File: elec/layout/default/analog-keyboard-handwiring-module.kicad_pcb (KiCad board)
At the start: 2 copper layers, 95.2 x 95.2 mm, 289 parts, among them J1 Conn_01x04, J10 Conn_01x02, J100 Conn_01x04, J11 Conn_01x01, J12 Conn_01x04, J13 Conn_01x04, J14 Conn_01x02, J15 Conn_01x01, J16 Conn_01x04, J17 Conn_01x04, J18 Conn_01x02, J19 Conn_01x01, J2 Conn_01x02, J20 Conn_01x04, J21 Conn_01x04, J22 Conn_01x02, J23 Conn_01x01, J24 Conn_01x04, J25 Conn_01x04, J26 Conn_01x02, J27 Conn_01x01, J28 Conn_01x04, J29 Conn_01x04, J3 Conn_01x01, J30 Conn_01x02, J31 Conn_01x01, J32 Conn_01x04, J33 Conn_01x04, J34 Conn_01x02, J35 Conn_01x01, J36 Conn_01x04, J37 Conn_01x04, J38 Conn_01x02, J39 Conn_01x01, J4 Conn_01x04, J40 Conn_01x04, J41 Conn_01x04, J42 Conn_01x02, J43 Conn_01x01, J44 Conn_01x04, J45 Conn_01x04, J46 Conn_01x02, J47 Conn_01x01, J48 Conn_01x04, J49 Conn_01x04, J5 Conn_01x04, J50 Conn_01x02, J51 Conn_01x01, J52 Conn_01x04, J53 Conn_01x04, J54 Conn_01x02, J55 Conn_01x01, J56 Conn_01x04, J57 Conn_01x04, J58 Conn_01x02, J59 Conn_01x01, J6 Conn_01x02, J60 Conn_01x04, J61 Conn_01x04, J62 Conn_01x02, J63 Conn_01x01, J64 Conn_01x04, J65 Conn_01x04, J66 Conn_01x02, J67 Conn_01x01, J68 Conn_01x04, J69 Conn_01x04, J7 Conn_01x01, J70 Conn_01x02, J71 Conn_01x01, J72 Conn_01x04, J73 Conn_01x04, J74 Conn_01x02, J75 Conn_01x01, J76 Conn_01x04, J77 Conn_01x04, J78 Conn_01x02, J79 Conn_01x01, J8 Conn_01x04, J80 Conn_01x04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

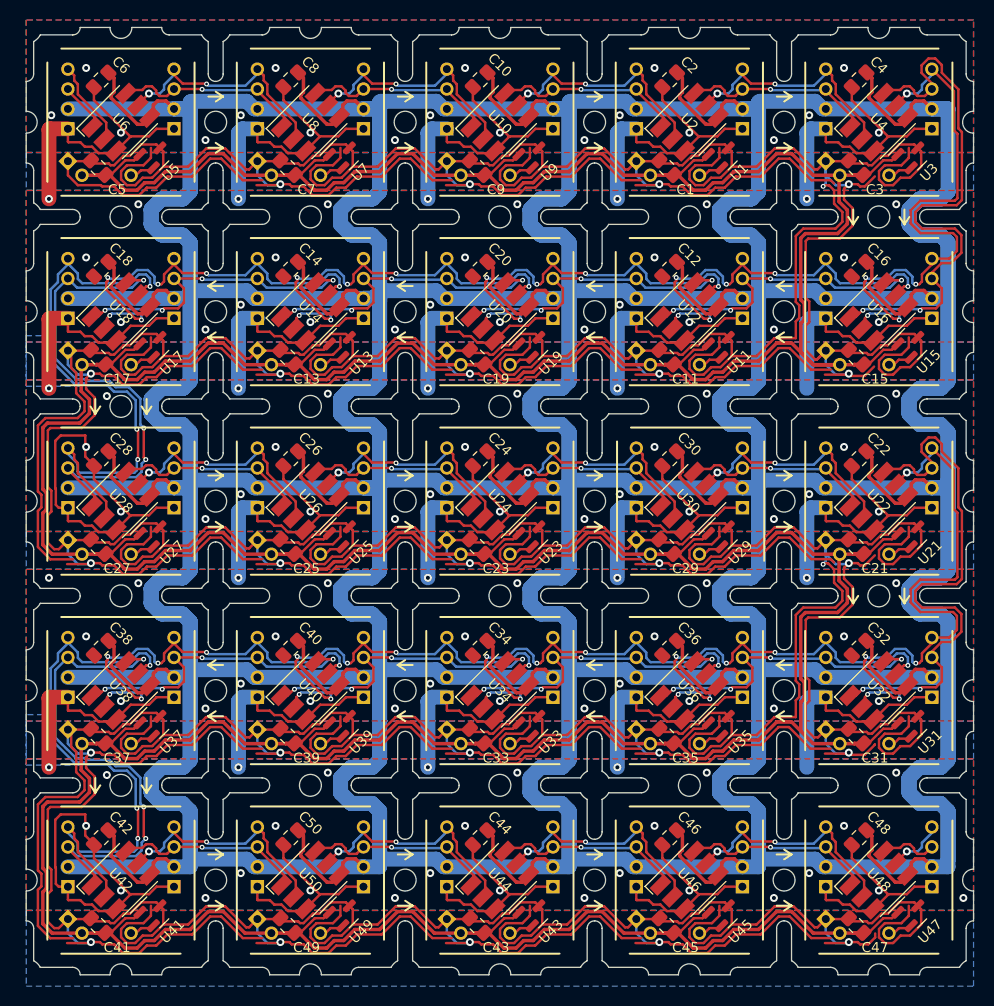
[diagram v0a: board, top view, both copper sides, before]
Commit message: Switch connectors and place components
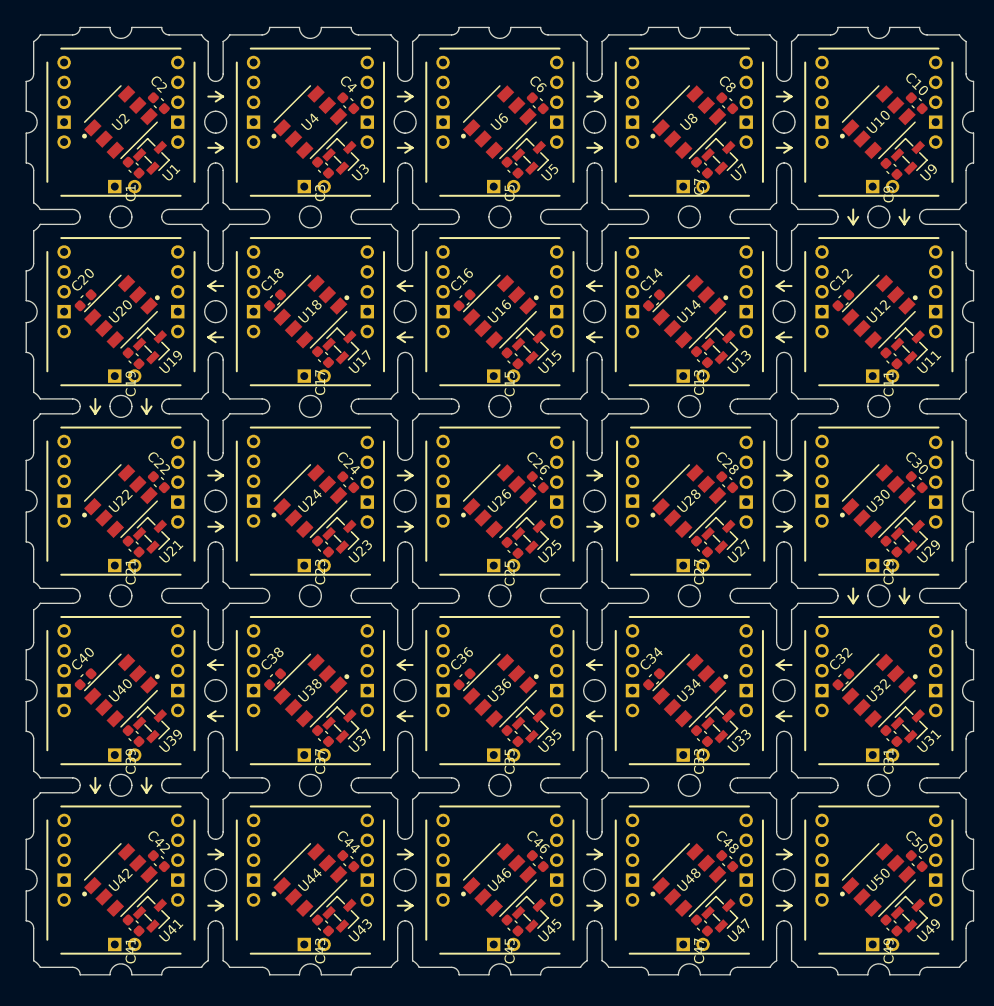
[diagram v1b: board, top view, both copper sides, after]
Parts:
- removed H1, H10, H11, H13, H14, H15, H16, H17, H19, H2, H20, H21, H22, H23, H24, H25, H26, H27, H28, H29, H3, H30, H31, H32, H33, H34, H35, H36, H37, H38, H39, H4, H40, H5, H6, H7, H8, H9, locked: MountingHole, MountingHole:MountingHole_2.2mm_M2
- removed H18: locked, MountingHole:MountingHole_2.2mm_M2
- removed the J10 at (92.3, 63.4)
- removed the J14 at (111.3, 63.4)
- removed the J18 at (130.4, 63.4)
- removed the J2 at (73.2, 63.4)
- removed the J22 at (130.4, 82.5)
- removed the J26 at (111.3, 82.5)
- removed the J30 at (92.3, 82.5)
- removed the J34 at (73.2, 82.5)
- removed the J38 at (54.2, 82.5)
- removed the J42 at (54.2, 101.5)
- removed the J46 at (73.2, 101.5)
- removed the J50 at (92.3, 101.5)
- removed the J54 at (111.3, 101.5)
- removed the J58 at (130.4, 101.5)
- removed the J6 at (54.2, 63.4)
- removed the J62 at (130.4, 120.6)
- removed the J66 at (111.3, 120.6)
- removed the J70 at (92.3, 120.6)
- removed the J74 at (73.2, 120.6)
- removed J78, J82, J86, J90, J94, J98: Conn_01x02, footprints:conn_2
- C1: renamed from C5; value 0.1µF -> 50V 100nF X7R ±10% 0603 Multilayer Ceramic Capacitors MLCC - SMD/SMT ROHS; footprint Capacitor_SMD:C_0805_2012Metric_Pad1.18x1.45mm_HandSolder -> lib:C0603
- C10: renamed from C4; value 0.1µF -> 50V 100nF X7R ±10% 0603 Multilayer Ceramic Capacitors MLCC - SMD/SMT ROHS; footprint Capacitor_SMD:C_0805_2012Metric_Pad1.18x1.45mm_HandSolder -> lib:C0603
- C11: renamed from C15; value 0.1µF -> 50V 100nF X7R ±10% 0603 Multilayer Ceramic Capacitors MLCC - SMD/SMT ROHS; footprint Capacitor_SMD:C_0805_2012Metric_Pad1.18x1.45mm_HandSolder -> lib:C0603
- C12: renamed from C16; value 0.1µF -> 50V 100nF X7R ±10% 0603 Multilayer Ceramic Capacitors MLCC - SMD/SMT ROHS; footprint Capacitor_SMD:C_0805_2012Metric_Pad1.18x1.45mm_HandSolder -> lib:C0603
- C13: renamed from C11; value 0.1µF -> 50V 100nF X7R ±10% 0603 Multilayer Ceramic Capacitors MLCC - SMD/SMT ROHS; footprint Capacitor_SMD:C_0805_2012Metric_Pad1.18x1.45mm_HandSolder -> lib:C0603
- C14: renamed from C12; value 0.1µF -> 50V 100nF X7R ±10% 0603 Multilayer Ceramic Capacitors MLCC - SMD/SMT ROHS; footprint Capacitor_SMD:C_0805_2012Metric_Pad1.18x1.45mm_HandSolder -> lib:C0603
- C15: renamed from C19; value 0.1µF -> 50V 100nF X7R ±10% 0603 Multilayer Ceramic Capacitors MLCC - SMD/SMT ROHS; footprint Capacitor_SMD:C_0805_2012Metric_Pad1.18x1.45mm_HandSolder -> lib:C0603
- C16: renamed from C20; value 0.1µF -> 50V 100nF X7R ±10% 0603 Multilayer Ceramic Capacitors MLCC - SMD/SMT ROHS; footprint Capacitor_SMD:C_0805_2012Metric_Pad1.18x1.45mm_HandSolder -> lib:C0603
- C17: renamed from C13; value 0.1µF -> 50V 100nF X7R ±10% 0603 Multilayer Ceramic Capacitors MLCC - SMD/SMT ROHS; footprint Capacitor_SMD:C_0805_2012Metric_Pad1.18x1.45mm_HandSolder -> lib:C0603
- C18: renamed from C14; value 0.1µF -> 50V 100nF X7R ±10% 0603 Multilayer Ceramic Capacitors MLCC - SMD/SMT ROHS; footprint Capacitor_SMD:C_0805_2012Metric_Pad1.18x1.45mm_HandSolder -> lib:C0603
- C19: renamed from C17; value 0.1µF -> 50V 100nF X7R ±10% 0603 Multilayer Ceramic Capacitors MLCC - SMD/SMT ROHS; footprint Capacitor_SMD:C_0805_2012Metric_Pad1.18x1.45mm_HandSolder -> lib:C0603
- C2: renamed from C6; value 0.1µF -> 50V 100nF X7R ±10% 0603 Multilayer Ceramic Capacitors MLCC - SMD/SMT ROHS; footprint Capacitor_SMD:C_0805_2012Metric_Pad1.18x1.45mm_HandSolder -> lib:C0603
- C20: renamed from C18; value 0.1µF -> 50V 100nF X7R ±10% 0603 Multilayer Ceramic Capacitors MLCC - SMD/SMT ROHS; footprint Capacitor_SMD:C_0805_2012Metric_Pad1.18x1.45mm_HandSolder -> lib:C0603
- C21: renamed from C27; value 0.1µF -> 50V 100nF X7R ±10% 0603 Multilayer Ceramic Capacitors MLCC - SMD/SMT ROHS; footprint Capacitor_SMD:C_0805_2012Metric_Pad1.18x1.45mm_HandSolder -> lib:C0603
- C22: renamed from C28; value 0.1µF -> 50V 100nF X7R ±10% 0603 Multilayer Ceramic Capacitors MLCC - SMD/SMT ROHS; footprint Capacitor_SMD:C_0805_2012Metric_Pad1.18x1.45mm_HandSolder -> lib:C0603
- C23: renamed from C25; value 0.1µF -> 50V 100nF X7R ±10% 0603 Multilayer Ceramic Capacitors MLCC - SMD/SMT ROHS; footprint Capacitor_SMD:C_0805_2012Metric_Pad1.18x1.45mm_HandSolder -> lib:C0603
- C24: renamed from C26; value 0.1µF -> 50V 100nF X7R ±10% 0603 Multilayer Ceramic Capacitors MLCC - SMD/SMT ROHS; footprint Capacitor_SMD:C_0805_2012Metric_Pad1.18x1.45mm_HandSolder -> lib:C0603
- C25: renamed from C23; value 0.1µF -> 50V 100nF X7R ±10% 0603 Multilayer Ceramic Capacitors MLCC - SMD/SMT ROHS; footprint Capacitor_SMD:C_0805_2012Metric_Pad1.18x1.45mm_HandSolder -> lib:C0603
- C26: renamed from C24; value 0.1µF -> 50V 100nF X7R ±10% 0603 Multilayer Ceramic Capacitors MLCC - SMD/SMT ROHS; footprint Capacitor_SMD:C_0805_2012Metric_Pad1.18x1.45mm_HandSolder -> lib:C0603
- C27: renamed from C29; value 0.1µF -> 50V 100nF X7R ±10% 0603 Multilayer Ceramic Capacitors MLCC - SMD/SMT ROHS; footprint Capacitor_SMD:C_0805_2012Metric_Pad1.18x1.45mm_HandSolder -> lib:C0603
- C28: renamed from C30; value 0.1µF -> 50V 100nF X7R ±10% 0603 Multilayer Ceramic Capacitors MLCC - SMD/SMT ROHS; footprint Capacitor_SMD:C_0805_2012Metric_Pad1.18x1.45mm_HandSolder -> lib:C0603
- C29: renamed from C21; value 0.1µF -> 50V 100nF X7R ±10% 0603 Multilayer Ceramic Capacitors MLCC - SMD/SMT ROHS; footprint Capacitor_SMD:C_0805_2012Metric_Pad1.18x1.45mm_HandSolder -> lib:C0603
- C3: renamed from C7; value 0.1µF -> 50V 100nF X7R ±10% 0603 Multilayer Ceramic Capacitors MLCC - SMD/SMT ROHS; footprint Capacitor_SMD:C_0805_2012Metric_Pad1.18x1.45mm_HandSolder -> lib:C0603
- C30: renamed from C22; value 0.1µF -> 50V 100nF X7R ±10% 0603 Multilayer Ceramic Capacitors MLCC - SMD/SMT ROHS; footprint Capacitor_SMD:C_0805_2012Metric_Pad1.18x1.45mm_HandSolder -> lib:C0603
- C31, C32, C41, C42: value 0.1µF -> 50V 100nF X7R ±10% 0603 Multilayer Ceramic Capacitors MLCC - SMD/SMT ROHS; footprint Capacitor_SMD:C_0805_2012Metric_Pad1.18x1.45mm_HandSolder -> lib:C0603
- C33: renamed from C35; value 0.1µF -> 50V 100nF X7R ±10% 0603 Multilayer Ceramic Capacitors MLCC - SMD/SMT ROHS; footprint Capacitor_SMD:C_0805_2012Metric_Pad1.18x1.45mm_HandSolder -> lib:C0603
- C34: renamed from C36; value 0.1µF -> 50V 100nF X7R ±10% 0603 Multilayer Ceramic Capacitors MLCC - SMD/SMT ROHS; footprint Capacitor_SMD:C_0805_2012Metric_Pad1.18x1.45mm_HandSolder -> lib:C0603
- C35: renamed from C33; value 0.1µF -> 50V 100nF X7R ±10% 0603 Multilayer Ceramic Capacitors MLCC - SMD/SMT ROHS; footprint Capacitor_SMD:C_0805_2012Metric_Pad1.18x1.45mm_HandSolder -> lib:C0603
- C36: renamed from C34; value 0.1µF -> 50V 100nF X7R ±10% 0603 Multilayer Ceramic Capacitors MLCC - SMD/SMT ROHS; footprint Capacitor_SMD:C_0805_2012Metric_Pad1.18x1.45mm_HandSolder -> lib:C0603
- C37: renamed from C39; value 0.1µF -> 50V 100nF X7R ±10% 0603 Multilayer Ceramic Capacitors MLCC - SMD/SMT ROHS; footprint Capacitor_SMD:C_0805_2012Metric_Pad1.18x1.45mm_HandSolder -> lib:C0603
- C38: renamed from C40; value 0.1µF -> 50V 100nF X7R ±10% 0603 Multilayer Ceramic Capacitors MLCC - SMD/SMT ROHS; footprint Capacitor_SMD:C_0805_2012Metric_Pad1.18x1.45mm_HandSolder -> lib:C0603
- C39: renamed from C37; value 0.1µF -> 50V 100nF X7R ±10% 0603 Multilayer Ceramic Capacitors MLCC - SMD/SMT ROHS; footprint Capacitor_SMD:C_0805_2012Metric_Pad1.18x1.45mm_HandSolder -> lib:C0603
- C4: renamed from C8; value 0.1µF -> 50V 100nF X7R ±10% 0603 Multilayer Ceramic Capacitors MLCC - SMD/SMT ROHS; footprint Capacitor_SMD:C_0805_2012Metric_Pad1.18x1.45mm_HandSolder -> lib:C0603
- C40: renamed from C38; value 0.1µF -> 50V 100nF X7R ±10% 0603 Multilayer Ceramic Capacitors MLCC - SMD/SMT ROHS; footprint Capacitor_SMD:C_0805_2012Metric_Pad1.18x1.45mm_HandSolder -> lib:C0603
- C43: renamed from C49; value 0.1µF -> 50V 100nF X7R ±10% 0603 Multilayer Ceramic Capacitors MLCC - SMD/SMT ROHS; footprint Capacitor_SMD:C_0805_2012Metric_Pad1.18x1.45mm_HandSolder -> lib:C0603
- C44: renamed from C50; value 0.1µF -> 50V 100nF X7R ±10% 0603 Multilayer Ceramic Capacitors MLCC - SMD/SMT ROHS; footprint Capacitor_SMD:C_0805_2012Metric_Pad1.18x1.45mm_HandSolder -> lib:C0603
- C45: renamed from C43; value 0.1µF -> 50V 100nF X7R ±10% 0603 Multilayer Ceramic Capacitors MLCC - SMD/SMT ROHS; footprint Capacitor_SMD:C_0805_2012Metric_Pad1.18x1.45mm_HandSolder -> lib:C0603
- C46: renamed from C44; value 0.1µF -> 50V 100nF X7R ±10% 0603 Multilayer Ceramic Capacitors MLCC - SMD/SMT ROHS; footprint Capacitor_SMD:C_0805_2012Metric_Pad1.18x1.45mm_HandSolder -> lib:C0603
- C47: renamed from C45; value 0.1µF -> 50V 100nF X7R ±10% 0603 Multilayer Ceramic Capacitors MLCC - SMD/SMT ROHS; footprint Capacitor_SMD:C_0805_2012Metric_Pad1.18x1.45mm_HandSolder -> lib:C0603
- C48: renamed from C46; value 0.1µF -> 50V 100nF X7R ±10% 0603 Multilayer Ceramic Capacitors MLCC - SMD/SMT ROHS; footprint Capacitor_SMD:C_0805_2012Metric_Pad1.18x1.45mm_HandSolder -> lib:C0603
- C49: renamed from C47; value 0.1µF -> 50V 100nF X7R ±10% 0603 Multilayer Ceramic Capacitors MLCC - SMD/SMT ROHS; footprint Capacitor_SMD:C_0805_2012Metric_Pad1.18x1.45mm_HandSolder -> lib:C0603
- C5: renamed from C9; value 0.1µF -> 50V 100nF X7R ±10% 0603 Multilayer Ceramic Capacitors MLCC - SMD/SMT ROHS; footprint Capacitor_SMD:C_0805_2012Metric_Pad1.18x1.45mm_HandSolder -> lib:C0603
- C50: renamed from C48; value 0.1µF -> 50V 100nF X7R ±10% 0603 Multilayer Ceramic Capacitors MLCC - SMD/SMT ROHS; footprint Capacitor_SMD:C_0805_2012Metric_Pad1.18x1.45mm_HandSolder -> lib:C0603
- C6: renamed from C10; value 0.1µF -> 50V 100nF X7R ±10% 0603 Multilayer Ceramic Capacitors MLCC - SMD/SMT ROHS; footprint Capacitor_SMD:C_0805_2012Metric_Pad1.18x1.45mm_HandSolder -> lib:C0603
- C7: renamed from C1; value 0.1µF -> 50V 100nF X7R ±10% 0603 Multilayer Ceramic Capacitors MLCC - SMD/SMT ROHS; footprint Capacitor_SMD:C_0805_2012Metric_Pad1.18x1.45mm_HandSolder -> lib:C0603
- C8: renamed from C2; value 0.1µF -> 50V 100nF X7R ±10% 0603 Multilayer Ceramic Capacitors MLCC - SMD/SMT ROHS; footprint Capacitor_SMD:C_0805_2012Metric_Pad1.18x1.45mm_HandSolder -> lib:C0603
- C9: renamed from C3; value 0.1µF -> 50V 100nF X7R ±10% 0603 Multilayer Ceramic Capacitors MLCC - SMD/SMT ROHS; footprint Capacitor_SMD:C_0805_2012Metric_Pad1.18x1.45mm_HandSolder -> lib:C0603
- J1: renamed from J5; value Conn_01x04 -> (none); footprint footprints:conn_4 -> lib:conn_inter
- J10: renamed from J13; value Conn_01x04 -> (none); footprint footprints:conn_4 -> lib:conn_inter
- J11: renamed from J16; value Conn_01x04 -> (none); footprint footprints:conn_4 -> lib:conn_inter
- J12: renamed from J15; value Conn_01x01 -> (none); footprint footprints:conn_1 -> lib:conn_2
- J13: renamed from J17; value Conn_01x04 -> (none); footprint footprints:conn_4 -> lib:conn_inter
- J14: renamed from J20; value Conn_01x04 -> (none); footprint footprints:conn_4 -> lib:conn_inter
- J15: renamed from J19; value Conn_01x01 -> (none); footprint footprints:conn_1 -> lib:conn_2
- J16: renamed from J21; value Conn_01x04 -> (none); footprint footprints:conn_4 -> lib:conn_inter
- J17: renamed from J24; value Conn_01x04 -> (none); footprint footprints:conn_4 -> lib:conn_inter
- J18: renamed from J23; value Conn_01x01 -> (none); footprint footprints:conn_1 -> lib:conn_2
- J19: renamed from J25; value Conn_01x04 -> (none); footprint footprints:conn_4 -> lib:conn_inter
- J2: renamed from J8; value Conn_01x04 -> (none); footprint footprints:conn_4 -> lib:conn_inter
- J20: renamed from J28; value Conn_01x04 -> (none); footprint footprints:conn_4 -> lib:conn_inter
- J21: renamed from J27; value Conn_01x01 -> (none); footprint footprints:conn_1 -> lib:conn_2
- J22: renamed from J29; value Conn_01x04 -> (none); footprint footprints:conn_4 -> lib:conn_inter
- J23: renamed from J32; value Conn_01x04 -> (none); footprint footprints:conn_4 -> lib:conn_inter
- J24: renamed from J31; value Conn_01x01 -> (none); footprint footprints:conn_1 -> lib:conn_2
- J25: renamed from J33; value Conn_01x04 -> (none); footprint footprints:conn_4 -> lib:conn_inter
- J26: renamed from J36; value Conn_01x04 -> (none); footprint footprints:conn_4 -> lib:conn_inter
- J27: renamed from J35; value Conn_01x01 -> (none); footprint footprints:conn_1 -> lib:conn_2
- J28: renamed from J37; value Conn_01x04 -> (none); footprint footprints:conn_4 -> lib:conn_inter
- J29: renamed from J40; value Conn_01x04 -> (none); footprint footprints:conn_4 -> lib:conn_inter
- J3: renamed from J7; value Conn_01x01 -> (none); footprint footprints:conn_1 -> lib:conn_2
- J30: renamed from J39; value Conn_01x01 -> (none); footprint footprints:conn_1 -> lib:conn_2
- J31: renamed from J41; value Conn_01x04 -> (none); footprint footprints:conn_4 -> lib:conn_inter
- J32: renamed from J44; value Conn_01x04 -> (none); footprint footprints:conn_4 -> lib:conn_inter
- J33: renamed from J43; value Conn_01x01 -> (none); footprint footprints:conn_1 -> lib:conn_2
- J34: renamed from J45; value Conn_01x04 -> (none); footprint footprints:conn_4 -> lib:conn_inter
- J35: renamed from J48; value Conn_01x04 -> (none); footprint footprints:conn_4 -> lib:conn_inter
- J36: renamed from J47; value Conn_01x01 -> (none); footprint footprints:conn_1 -> lib:conn_2
- J37: renamed from J49; value Conn_01x04 -> (none); footprint footprints:conn_4 -> lib:conn_inter
- J38: renamed from J52; value Conn_01x04 -> (none); footprint footprints:conn_4 -> lib:conn_inter
- J39: renamed from J51; value Conn_01x01 -> (none); footprint footprints:conn_1 -> lib:conn_2
- J4: renamed from J1; value Conn_01x04 -> (none); footprint footprints:conn_4 -> lib:conn_inter
- J40: renamed from J53; value Conn_01x04 -> (none); footprint footprints:conn_4 -> lib:conn_inter
- J41: renamed from J56; value Conn_01x04 -> (none); footprint footprints:conn_4 -> lib:conn_inter
- J42: renamed from J55; value Conn_01x01 -> (none); footprint footprints:conn_1 -> lib:conn_2
- J43: renamed from J57; value Conn_01x04 -> (none); footprint footprints:conn_4 -> lib:conn_inter
- J44: renamed from J60; value Conn_01x04 -> (none); footprint footprints:conn_4 -> lib:conn_inter
- J45: renamed from J59; value Conn_01x01 -> (none); footprint footprints:conn_1 -> lib:conn_2
- J46: renamed from J61; value Conn_01x04 -> (none); footprint footprints:conn_4 -> lib:conn_inter
- J47: renamed from J64; value Conn_01x04 -> (none); footprint footprints:conn_4 -> lib:conn_inter
- J48: renamed from J63; value Conn_01x01 -> (none); footprint footprints:conn_1 -> lib:conn_2
- J49: renamed from J65; value Conn_01x04 -> (none); footprint footprints:conn_4 -> lib:conn_inter
- J5: renamed from J4; value Conn_01x04 -> (none); footprint footprints:conn_4 -> lib:conn_inter
- J50: renamed from J68; value Conn_01x04 -> (none); footprint footprints:conn_4 -> lib:conn_inter
- J51: renamed from J67; value Conn_01x01 -> (none); footprint footprints:conn_1 -> lib:conn_2
- J52: renamed from J69; value Conn_01x04 -> (none); footprint footprints:conn_4 -> lib:conn_inter
- J53: renamed from J72; value Conn_01x04 -> (none); footprint footprints:conn_4 -> lib:conn_inter
- J54: renamed from J71; value Conn_01x01 -> (none); footprint footprints:conn_1 -> lib:conn_2
- J55: renamed from J73; value Conn_01x04 -> (none); footprint footprints:conn_4 -> lib:conn_inter
- J56: renamed from J76; value Conn_01x04 -> (none); footprint footprints:conn_4 -> lib:conn_inter
- J57: renamed from J75; value Conn_01x01 -> (none); footprint footprints:conn_1 -> lib:conn_2
- J58: renamed from J77; value Conn_01x04 -> (none); footprint footprints:conn_4 -> lib:conn_inter
- J59: renamed from J80; value Conn_01x04 -> (none); footprint footprints:conn_4 -> lib:conn_inter
- J6: renamed from J3; value Conn_01x01 -> (none); footprint footprints:conn_1 -> lib:conn_2
- J60: renamed from J79; value Conn_01x01 -> (none); footprint footprints:conn_1 -> lib:conn_2
- J61: renamed from J81; value Conn_01x04 -> (none); footprint footprints:conn_4 -> lib:conn_inter
- J62: renamed from J84; value Conn_01x04 -> (none); footprint footprints:conn_4 -> lib:conn_inter
- J63: renamed from J83; value Conn_01x01 -> (none); footprint footprints:conn_1 -> lib:conn_2
- J64: renamed from J85; value Conn_01x04 -> (none); footprint footprints:conn_4 -> lib:conn_inter
- J65: renamed from J88; value Conn_01x04 -> (none); footprint footprints:conn_4 -> lib:conn_inter
- J66: renamed from J87; value Conn_01x01 -> (none); footprint footprints:conn_1 -> lib:conn_2
- J67: renamed from J89; value Conn_01x04 -> (none); footprint footprints:conn_4 -> lib:conn_inter
- J68: renamed from J92; value Conn_01x04 -> (none); footprint footprints:conn_4 -> lib:conn_inter
- J69: renamed from J91; value Conn_01x01 -> (none); footprint footprints:conn_1 -> lib:conn_2
- J7: renamed from J9; value Conn_01x04 -> (none); footprint footprints:conn_4 -> lib:conn_inter
- J70: renamed from J93; value Conn_01x04 -> (none); footprint footprints:conn_4 -> lib:conn_inter
- J71: renamed from J96; value Conn_01x04 -> (none); footprint footprints:conn_4 -> lib:conn_inter
- J72: renamed from J95; value Conn_01x01 -> (none); footprint footprints:conn_1 -> lib:conn_2
- J73: renamed from J97; value Conn_01x04 -> (none); footprint footprints:conn_4 -> lib:conn_inter
- J74: renamed from J100; value Conn_01x04 -> (none); footprint footprints:conn_4 -> lib:conn_inter
- J75: renamed from J99; value Conn_01x01 -> (none); footprint footprints:conn_1 -> lib:conn_2
- J8: renamed from J12; value Conn_01x04 -> (none); footprint footprints:conn_4 -> lib:conn_inter
- J9: renamed from J11; value Conn_01x01 -> (none); footprint footprints:conn_1 -> lib:conn_2
- N1: renamed from N3; value VoidSwitch Footprint -> (none); footprint footprints:VoidSwitch -> lib:VoidSwitch
- N10, N12, N14, N16, N18, N2, N20, N22, N24, N26, N28, N30, N32, N34, N36, N38, N4, N40, N42, N44, N46, N48, N6, N8: renamed from REF**; value arrows -> (none); footprint footprints:arrows -> lib:arrows
- N11: renamed from N8; value VoidSwitch Footprint -> (none); footprint footprints:VoidSwitch -> lib:VoidSwitch
- N13: renamed from N6; value VoidSwitch Footprint -> (none); footprint footprints:VoidSwitch -> lib:VoidSwitch
- N15: renamed from N10; value VoidSwitch Footprint -> (none); footprint footprints:VoidSwitch -> lib:VoidSwitch
- N17: renamed from N7; value VoidSwitch Footprint -> (none); footprint footprints:VoidSwitch -> lib:VoidSwitch
- N19: renamed from N9; value VoidSwitch Footprint -> (none); footprint footprints:VoidSwitch -> lib:VoidSwitch
- N21: renamed from N14; value VoidSwitch Footprint -> (none); footprint footprints:VoidSwitch -> lib:VoidSwitch
- N23: renamed from N13; value VoidSwitch Footprint -> (none); footprint footprints:VoidSwitch -> lib:VoidSwitch
- N25: renamed from N12; value VoidSwitch Footprint -> (none); footprint footprints:VoidSwitch -> lib:VoidSwitch
- N27: renamed from N15; value VoidSwitch Footprint -> (none); footprint footprints:VoidSwitch -> lib:VoidSwitch
- N29: renamed from N11; value VoidSwitch Footprint -> (none); footprint footprints:VoidSwitch -> lib:VoidSwitch
- N3: renamed from N4; value VoidSwitch Footprint -> (none); footprint footprints:VoidSwitch -> lib:VoidSwitch
- N31: renamed from N16; value VoidSwitch Footprint -> (none); footprint footprints:VoidSwitch -> lib:VoidSwitch
- N33: renamed from N18; value VoidSwitch Footprint -> (none); footprint footprints:VoidSwitch -> lib:VoidSwitch
- N35: renamed from N17; value VoidSwitch Footprint -> (none); footprint footprints:VoidSwitch -> lib:VoidSwitch
- N37: renamed from N20; value VoidSwitch Footprint -> (none); footprint footprints:VoidSwitch -> lib:VoidSwitch
- N39: renamed from N19; value VoidSwitch Footprint -> (none); footprint footprints:VoidSwitch -> lib:VoidSwitch
- N41: renamed from N21; value VoidSwitch Footprint -> (none); footprint footprints:VoidSwitch -> lib:VoidSwitch
- N43: renamed from N25; value VoidSwitch Footprint -> (none); footprint footprints:VoidSwitch -> lib:VoidSwitch
- N45: renamed from N22; value VoidSwitch Footprint -> (none); footprint footprints:VoidSwitch -> lib:VoidSwitch
- N47: renamed from N23; value VoidSwitch Footprint -> (none); footprint footprints:VoidSwitch -> lib:VoidSwitch
- N49: renamed from N24; value VoidSwitch Footprint -> (none); footprint footprints:VoidSwitch -> lib:VoidSwitch
- N5: value VoidSwitch Footprint -> (none); footprint footprints:VoidSwitch -> lib:VoidSwitch
- N7: renamed from N1; value VoidSwitch Footprint -> (none); footprint footprints:VoidSwitch -> lib:VoidSwitch
- N9: renamed from N2; value VoidSwitch Footprint -> (none); footprint footprints:VoidSwitch -> lib:VoidSwitch
- U1: renamed from U5; value Hall Sensor -> (none); footprint Package_TO_SOT_SMD:SOT-23 -> lib:SOT-23-3_L2.9-W1.3-P1.90-LS2.4-BR
- U10: renamed from U4; value SK9822 -> (none); footprint LED_SMD:LED_RGB_5050-6 -> lib:SMD_6P-L5.0-W5.0-TL
- U11: renamed from U15; value Hall Sensor -> (none); footprint Package_TO_SOT_SMD:SOT-23 -> lib:SOT-23-3_L2.9-W1.3-P1.90-LS2.4-BR
- U12: renamed from U16; value SK9822 -> (none); footprint LED_SMD:LED_RGB_5050-6 -> lib:SMD_6P-L5.0-W5.0-TL
- U13: renamed from U11; value Hall Sensor -> (none); footprint Package_TO_SOT_SMD:SOT-23 -> lib:SOT-23-3_L2.9-W1.3-P1.90-LS2.4-BR
- U14: renamed from U12; value SK9822 -> (none); footprint LED_SMD:LED_RGB_5050-6 -> lib:SMD_6P-L5.0-W5.0-TL
- U15: renamed from U19; value Hall Sensor -> (none); footprint Package_TO_SOT_SMD:SOT-23 -> lib:SOT-23-3_L2.9-W1.3-P1.90-LS2.4-BR
- U16: renamed from U20; value SK9822 -> (none); footprint LED_SMD:LED_RGB_5050-6 -> lib:SMD_6P-L5.0-W5.0-TL
- U17: renamed from U13; value Hall Sensor -> (none); footprint Package_TO_SOT_SMD:SOT-23 -> lib:SOT-23-3_L2.9-W1.3-P1.90-LS2.4-BR
- U18: renamed from U14; value SK9822 -> (none); footprint LED_SMD:LED_RGB_5050-6 -> lib:SMD_6P-L5.0-W5.0-TL
- U19: renamed from U17; value Hall Sensor -> (none); footprint Package_TO_SOT_SMD:SOT-23 -> lib:SOT-23-3_L2.9-W1.3-P1.90-LS2.4-BR
- U2: renamed from U6; value SK9822 -> (none); footprint LED_SMD:LED_RGB_5050-6 -> lib:SMD_6P-L5.0-W5.0-TL
- U20: renamed from U18; value SK9822 -> (none); footprint LED_SMD:LED_RGB_5050-6 -> lib:SMD_6P-L5.0-W5.0-TL
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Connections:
- net /Module/SDI_LED renamed ck
- net /Module/SDO_LED renamed row1.key1-ck
- net /Module1/SDO_LED renamed row1.key2-ck
- net /Module10/SDO_LED renamed row3.key1-ck
- net /Module11/SDO_LED renamed row3.key2-ck
- net /Module12/SDO_LED renamed row3.key3-ck
- net /Module15/SDO_LED renamed row4.key1-ck
- net /Module16/SDO_LED renamed row4.key2-ck
- net /Module17/SDO_LED renamed row4.key3-ck
- net /Module2/SDO_LED renamed row1.key3-ck
- net /Module20/SDO_LED renamed row5.key1-ck
- net /Module21/SDO_LED renamed row5.key2-ck
- net /Module22/SDO_LED renamed row5.key3-ck
- net /Module23/SDI_LED renamed row5-ck
- net /Module23/SDO_LED renamed row5.key5-ck
- net /Module5/SDO_LED renamed row2.key1-ck
- net /Module6/SDO_LED renamed row2.key2-ck
- net /Module7/SDO_LED renamed row2.key3-ck
- C1 pad 1: GND_HALL -> vcch
- C1 pad 2: V_HALL -> gnd
- C10 pad 1: V_LED -> vccl
- C10 pad 2: GND_LED -> gnd
- C11 pad 1: GND_HALL -> vcch
- C11 pad 2: V_HALL -> gnd
- C12 pad 1: V_LED -> vccl
- C12 pad 2: GND_LED -> gnd
- C13 pad 1: GND_HALL -> vcch
- C13 pad 2: V_HALL -> gnd
- C14 pad 1: V_LED -> vccl
- C14 pad 2: GND_LED -> gnd
- C15 pad 1: GND_HALL -> vcch
- C15 pad 2: V_HALL -> gnd
- C16 pad 1: V_LED -> vccl
- C16 pad 2: GND_LED -> gnd
- C17 pad 1: GND_HALL -> vcch
- C17 pad 2: V_HALL -> gnd
- C18 pad 1: V_LED -> vccl
- C18 pad 2: GND_LED -> gnd
- C19 pad 1: GND_HALL -> vcch
- C19 pad 2: V_HALL -> gnd
- C2 pad 1: V_LED -> vccl
- C2 pad 2: GND_LED -> gnd
- C20 pad 1: V_LED -> vccl
- C20 pad 2: GND_LED -> gnd
- C21 pad 1: GND_HALL -> vcch
- C21 pad 2: V_HALL -> gnd
- C22 pad 1: V_LED -> vccl
- C22 pad 2: GND_LED -> gnd
- C23 pad 1: GND_HALL -> vcch
- C23 pad 2: V_HALL -> gnd
- C24 pad 1: V_LED -> vccl
- C24 pad 2: GND_LED -> gnd
- C25 pad 1: GND_HALL -> vcch
- C25 pad 2: V_HALL -> gnd
- C26 pad 1: V_LED -> vccl
- C26 pad 2: GND_LED -> gnd
- C27 pad 1: GND_HALL -> vcch
- C27 pad 2: V_HALL -> gnd
- C28 pad 1: V_LED -> vccl
- C28 pad 2: GND_LED -> gnd
- C29 pad 1: GND_HALL -> vcch
- C29 pad 2: V_HALL -> gnd
- C3 pad 1: GND_HALL -> vcch
- C3 pad 2: V_HALL -> gnd
- C30 pad 1: V_LED -> vccl
- C30 pad 2: GND_LED -> gnd
- C31 pad 1: GND_HALL -> vcch
- C31 pad 2: V_HALL -> gnd
- C32 pad 1: V_LED -> vccl
- C32 pad 2: GND_LED -> gnd
- C33 pad 1: GND_HALL -> vcch
- C33 pad 2: V_HALL -> gnd
- C34 pad 1: V_LED -> vccl
- C34 pad 2: GND_LED -> gnd
- C35 pad 1: GND_HALL -> vcch
- C35 pad 2: V_HALL -> gnd
- C36 pad 1: V_LED -> vccl
- C36 pad 2: GND_LED -> gnd
- C37 pad 1: GND_HALL -> vcch
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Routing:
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- removed copper zone on B.Cu, net GND_HALL
- removed copper zone on B.Cu, net GND_LED
- removed copper zone on F.Cu, net GND_LED
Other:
- outline, holes or cut-outs redrawn
- board text added: "GND"
- board text removed: "GLED"
- board text removed: "GNDH"
- board text removed: "GNDL"
- board text removed: "HALL"

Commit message: Fix component and designator placement
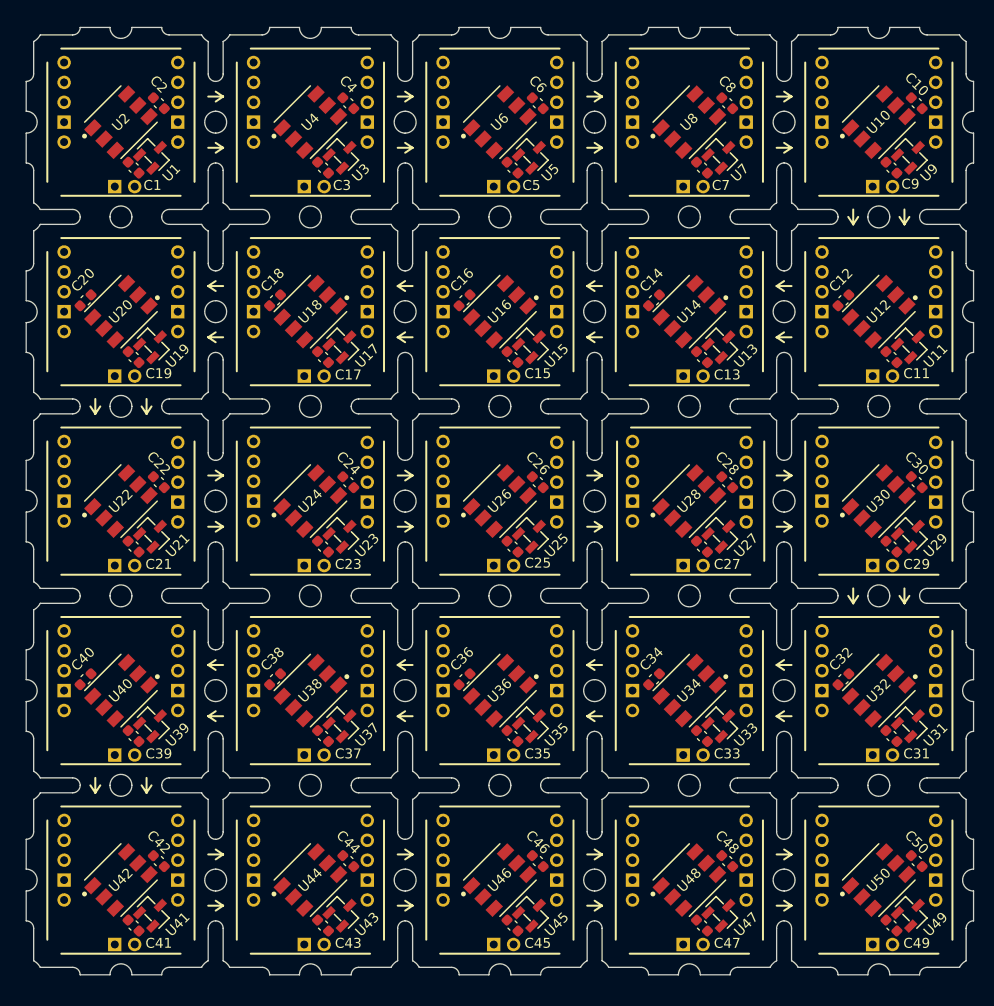
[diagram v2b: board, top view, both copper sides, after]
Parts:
- moved C9 0.13 mm to (137.0, 64.1)
- moved C11 0.13 mm to (137.0, 83.1)
- moved C15 0.13 mm to (98.9, 83.1)
- moved C19 0.13 mm to (60.8, 83.1)
- moved C25 0.13 mm to (98.9, 102.2)
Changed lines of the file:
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@@
 		(allow_soldermask_bridges_in_footprints no)
 		(aux_axis_origin 50 50)
-		(grid_origin 58.906 66.002)
+		(grid_origin 60.795 64.097)
 		(pcbplotparams
 			(layerselection 0x00010fc_ffffffff)
@@
 		(tags "capacitor")
 		(property "Reference" "C13"
-			(at 1.616446 1.975656 90)
+			(at 3.053287 -0.538815 180)
 			(layer "F.SilkS")
 			(effects
@@
 		(at 100.875 119.925 -135)
 		(property "Reference" "U35"
-			(at 0 -2.588011 -135)
+			(at -0.898026 -2.588011 -135)
 			(layer "F.SilkS")
 			(effects
@@
 		(tags "capacitor")
 		(property "Reference" "C35"
-			(at 1.616446 1.975656 90)
+			(at 3.053287 -0.538815 180)
 			(layer "F.SilkS")
 			(effects
@@
 		(tags "capacitor")
 		(property "Reference" "C49"
-			(at 1.616446 1.975656 90)
+			(at 3.053287 -0.538815 180)
 			(layer "F.SilkS")
 			(effects
@@
 	(footprint "lib:C0603"
 		(layer "F.Cu")
-		(at 60.795 83.274 -45)
+		(at 60.795 83.147 -45)
 		(descr "Capacitor SMD 0603 (1608 Metric), square (rectangular) end terminal, IPC_7351 nominal, (Body size source: IPC-SM-782 page 76, https://www.pcb-3d.com/wordpress/wp-content/uploads/ipc-sm-782a_amendment_1_and_2.pdf), generated with kicad-footprint-generator")
 		(tags "capacitor")
 		(property "Reference" "C19"
-			(at 1.616446 1.975656 90)
+			(at 2.963485 -0.628618 180)
 			(layer "F.SilkS")
 			(effects
@@
 		(at 100.875 81.825 -135)
 		(property "Reference" "U15"
-			(at 0 -2.588011 -135)
+			(at -0.898026 -2.588011 -135)
 			(layer "F.SilkS")
 			(effects
@@
 		(at 138.975 119.925 -135)
 		(property "Reference" "U31"
-			(at 0 -2.588011 -135)
+			(at -0.898026 -2.588011 -135)
 			(layer "F.SilkS")
 			(effects
@@
 	(footprint "lib:C0603"
 		(layer "F.Cu")
-		(at 98.895 83.274 -45)
+		(at 98.895 83.147 -45)
 		(descr "Capacitor SMD 0603 (1608 Metric), square (rectangular) end terminal, IPC_7351 nominal, (Body size source: IPC-SM-782 page 76, https://www.pcb-3d.com/wordpress/wp-content/uploads/ipc-sm-782a_amendment_1_and_2.pdf), generated with kicad-footprint-generator")
 		(tags "capacitor")
 		(property "Reference" "C15"
-			(at 1.616446 1.975656 90)
+			(at 2.963485 -0.628618 180)
 			(layer "F.SilkS")
 			(effects
@@
 		(at 62.775 138.975 -135)
 		(property "Reference" "U41"
-			(at 0 -2.588011 -135)
+			(at -0.898026 -2.588011 -135)
 			(layer "F.SilkS")
 			(effects
@@
 		(at 81.825 119.925 -135)
 		(property "Reference" "U37"
-			(at 0 -2.588011 -135)
+			(at -0.898026 -2.588011 -135)
 			(layer "F.SilkS")
 			(effects
@@
 	(footprint "lib:C0603"
 		(layer "F.Cu")
-		(at 136.995 83.274 -45)
+		(at 136.995 83.147 -45)
 		(descr "Capacitor SMD 0603 (1608 Metric), square (rectangular) end terminal, IPC_7351 nominal, (Body size source: IPC-SM-782 page 76, https://www.pcb-3d.com/wordpress/wp-content/uploads/ipc-sm-782a_amendment_1_and_2.pdf), generated with kicad-footprint-generator")
 		(tags "capacitor")
 		(property "Reference" "C11"
-			(at 1.616446 1.975656 90)
+			(at 2.963485 -0.628618 180)
 			(layer "F.SilkS")
 			(effects
@@
 		(at 100.875 138.975 -135)
 		(property "Reference" "U45"
-			(at 0 -2.588011 -135)
+			(at -0.898026 -2.588011 -135)
 			(layer "F.SilkS")
 			(effects
@@
 		(at 119.925 119.925 -135)
 		(property "Reference" "U33"
-			(at 0 -2.588011 -135)
+			(at -0.898026 -2.588011 -135)
 			(layer "F.SilkS")
 			(effects
@@
 		(tags "capacitor")
 		(property "Reference" "C7"
-			(at 1.167433 1.526644 90)
+			(at 2.604274 -0.089803 180)
 			(layer "F.SilkS")
 			(effects
@@
 		(at 119.925 100.875 -135)
 		(property "Reference" "U27"
-			(at 0 -2.588011 -135)
+			(at -0.898026 -2.588011 -135)
 			(layer "F.SilkS")
 			(effects
@@
 		(tags "capacitor")
 		(property "Reference" "C5"
-			(at 1.616446 1.975656 90)
+			(at 2.604274 -0.089803 180)
 			(layer "F.SilkS")
 			(effects
@@
 		(tags "capacitor")
 		(property "Reference" "C17"
-			(at 1.616446 1.975656 90)
+			(at 3.053287 -0.538815 180)
 			(layer "F.SilkS")
 			(effects
@@
 		(tags "capacitor")
 		(property "Reference" "C31"
-			(at 1.616446 1.975656 90)
+			(at 3.053287 -0.538815 180)
 			(layer "F.SilkS")
 			(effects
@@
 		(at 81.825 100.875 -135)
 		(property "Reference" "U23"
-			(at 0 -2.588011 -135)
+			(at -0.898026 -2.588011 -135)
 			(layer "F.SilkS")
 			(effects
@@
 		(at 62.775 100.875 -135)
 		(property "Reference" "U21"
-			(at 0 -2.588011 -135)
+			(at -0.898026 -2.588011 -135)
 			(layer "F.SilkS")
 			(effects
@@
 		(tags "capacitor")
 		(property "Reference" "C45"
-			(at 1.616446 1.975656 90)
+			(at 3.053287 -0.538815 180)
 			(layer "F.SilkS")
 			(effects
@@
 		(at 81.825 81.825 -135)
 		(property "Reference" "U17"
-			(at 0 -2.588011 -135)
+			(at -0.898026 -2.588011 -135)
 			(layer "F.SilkS")
 			(effects
@@
 		(tags "capacitor")
 		(property "Reference" "C1"
-			(at 1.616446 1.975656 90)
+			(at 2.604274 -0.089803 180)
 			(layer "F.SilkS")
 			(effects
@@
 		(at 119.925 138.975 -135)
 		(property "Reference" "U47"
-			(at 0 -2.588011 -135)
+			(at -0.898026 -2.588011 -135)
 			(layer "F.SilkS")
 			(effects
@@
 		(tags "capacitor")
 		(property "Reference" "C43"
-			(at 1.616446 1.975656 90)
+			(at 3.053287 -0.538815 180)
 			(layer "F.SilkS")
 			(effects
@@
 		(tags "capacitor")
 		(property "Reference" "C33"
-			(at 1.616446 1.975656 90)
+			(at 3.053287 -0.538815 180)
 			(layer "F.SilkS")
 			(effects
@@
 		(tags "capacitor")
 		(property "Reference" "C23"
-			(at 1.616446 1.975656 90)
+			(at 3.053287 -0.538815 180)
 			(layer "F.SilkS")
 			(effects
@@
 		(tags "capacitor")
 		(property "Reference" "C37"
-			(at 1.616446 1.975656 90)
+			(at 3.053287 -0.538815 180)
 			(layer "F.SilkS")
 			(effects
@@
 	(footprint "lib:C0603"
 		(layer "F.Cu")
-		(at 98.895 102.324 -45)
+		(at 98.895 102.197 -45)
 		(descr "Capacitor SMD 0603 (1608 Metric), square (rectangular) end terminal, IPC_7351 nominal, (Body size source: IPC-SM-782 page 76, https://www.pcb-3d.com/wordpress/wp-content/uploads/ipc-sm-782a_amendment_1_and_2.pdf), generated with kicad-footprint-generator")
 		(tags "capacitor")
 		(property "Reference" "C25"
-			(at 1.616446 1.975656 90)
+			(at 2.963485 -0.628618 180)
 			(layer "F.SilkS")
 			(effects
@@
 		(tags "capacitor")
 		(property "Reference" "C41"
-			(at 1.616446 1.975656 90)
+			(at 3.053287 -0.538815 180)
 			(layer "F.SilkS")
 			(effects
@@
 		(at 119.925 81.825 -135)
 		(property "Reference" "U13"
-			(at 0 -2.588011 -135)
+			(at -0.898026 -2.588011 -135)
 			(layer "F.SilkS")
 			(effects
@@
 		(at 138.975 81.825 -135)
 		(property "Reference" "U11"
-			(at 0 -2.588011 -135)
+			(at -0.898026 -2.588011 -135)
 			(layer "F.SilkS")
 			(effects
@@
 		(at 138.975 100.875 -135)
 		(property "Reference" "U29"
-			(at 0 -2.588011 -135)
+			(at -0.898026 -2.588011 -135)
 			(layer "F.SilkS")
 			(effects
@@
 		(tags "capacitor")
 		(property "Reference" "C21"
-			(at 1.616446 1.975656 90)
+			(at 3.053287 -0.538815 180)
 			(layer "F.SilkS")
 			(effects
@@
 		(at 62.775 81.825 -135)
 		(property "Reference" "U19"
-			(at 0 -2.588011 -135)
+			(at -0.898026 -2.588011 -135)
 			(layer "F.SilkS")
 			(effects
@@
 		(tags "capacitor")
 		(property "Reference" "C39"
-			(at 1.616446 1.975656 90)
+			(at 3.053287 -0.538815 180)
 			(layer "F.SilkS")
 			(effects
@@
 		(tags "capacitor")
 		(property "Reference" "C29"
-			(at 1.616446 1.975656 90)
+			(at 3.053287 -0.538815 180)
 			(layer "F.SilkS")
 			(effects
@@
 		(at 100.875 100.875 -135)
 		(property "Reference" "U25"
-			(at 0 -2.588011 -135)
+			(at -0.898026 -2.588011 -135)
 			(layer "F.SilkS")
 			(effects
@@
 		(at 138.975 138.975 -135)
 		(property "Reference" "U49"
-			(at 0 -2.588011 -135)
+			(at -0.898026 -2.588011 -135)
 			(layer "F.SilkS")
 			(effects
@@
 		(tags "capacitor")
 		(property "Reference" "C3"
-			(at 1.616446 1.975656 90)
+			(at 2.604274 -0.089803 180)
 			(layer "F.SilkS")
 			(effects
@@
 		(at 81.825 138.975 -135)
 		(property "Reference" "U43"
-			(at 0 -2.588011 -135)
+			(at -0.898026 -2.588011 -135)
 			(layer "F.SilkS")
 			(effects
@@
 		(tags "capacitor")
 		(property "Reference" "C47"
-			(at 1.616446 1.975656 90)
+			(at 3.053287 -0.538815 180)
 			(layer "F.SilkS")
 			(effects
@@
 	(footprint "lib:C0603"
 		(layer "F.Cu")
-		(at 136.995 64.224 -45)
+		(at 136.995 64.097 -45)
 		(descr "Capacitor SMD 0603 (1608 Metric), square (rectangular) end terminal, IPC_7351 nominal, (Body size source: IPC-SM-782 page 76, https://www.pcb-3d.com/wordpress/wp-content/uploads/ipc-sm-782a_amendment_1_and_2.pdf), generated with kicad-footprint-generator")
 		(tags "capacitor")
 		(property "Reference" "C9"
-			(at 1.616446 1.975656 90)
+			(at 2.514472 -0.179605 180)
 			(layer "F.SilkS")
 			(effects
@@
 		(at 62.775 119.925 -135)
 		(property "Reference" "U39"
-			(at 0 -2.588011 -135)
+			(at -0.898026 -2.588011 -135)
 			(layer "F.SilkS")
 			(effects
@@
 		(tags "capacitor")
 		(property "Reference" "C27"
-			(at 1.616446 1.975656 90)
+			(at 3.053287 -0.538815 180)
 			(layer "F.SilkS")
 			(effects
